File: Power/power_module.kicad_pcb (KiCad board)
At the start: 4 copper layers, 198 x 88 mm, 54 parts, among them J1 Conn_02x03_Odd_Even, J10 Conn_01x04, J11 Conn_02x02_Odd_Even, J2 Conn_02x03_Odd_Even, J3 Conn_02x06_Counter_Clockwise, J4 Conn_02x05_Top_Bottom, J5 Conn_02x05_Top_Bottom, J6 Conn_02x02_Odd_Even, J7 Conn_02x02_Odd_Even, J8 Conn_01x06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

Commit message: Mosfet konumlari degistirildi. Layout iyilestirme yapildi.
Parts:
- moved Q1 22.9 mm to (238.8, 110.5), turned to 270 degrees
- moved D2 16.7 mm to (238.1, 106.5)
- moved R31 12.7 mm to (238.5, 104.1), turned to 180 degrees
- moved D3 11.6 mm to (228.5, 106.6), turned to 180 degrees
- moved R14 11.2 mm to (238.5, 101.7), turned to 0 degrees
- moved Q2 11.0 mm to (227.5, 121.4), turned to 90 degrees
- moved D4 10.2 mm to (241.2, 131.3), turned to 180 degrees
- moved R32 7.43 mm to (228.2, 104.2), turned to 0 degrees
- moved R19 6.72 mm to (228.2, 101.8), turned to 180 degrees
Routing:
- net /CrtPad: track 18.2 -> 83.7 mm
- net GNDA: track 227.4 -> 255.8 mm, vias 10 -> 22
- net /Vout+: track 217.0 -> 234.0 mm
- net Vin_Sens: track 89.9 -> 95.3 mm
- net /Gate2: track 11.3 -> 8.31 mm, vias 0 -> 4
- net /Bridge-: track 121.0 -> 123.8 mm
- net /Gate1: track 12.0 -> 10.6 mm, vias 1 -> 6
- net /Drv_Out: track 14.8 -> 15.6 mm
- net (no net): vias 5 -> 0
- added copper zone on B.Cu, net /CrtPad
- added copper zone on In1.Cu, net /Gate2
- added copper zone on B.Cu, net /Line1
- added copper zone on In2.Cu, net /Line1
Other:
- net class Bridge: clearance 0.8 -> 3
- net class GNDA: clearance 0.3 -> 3
- net class Phase: clearance 0.8 -> 3

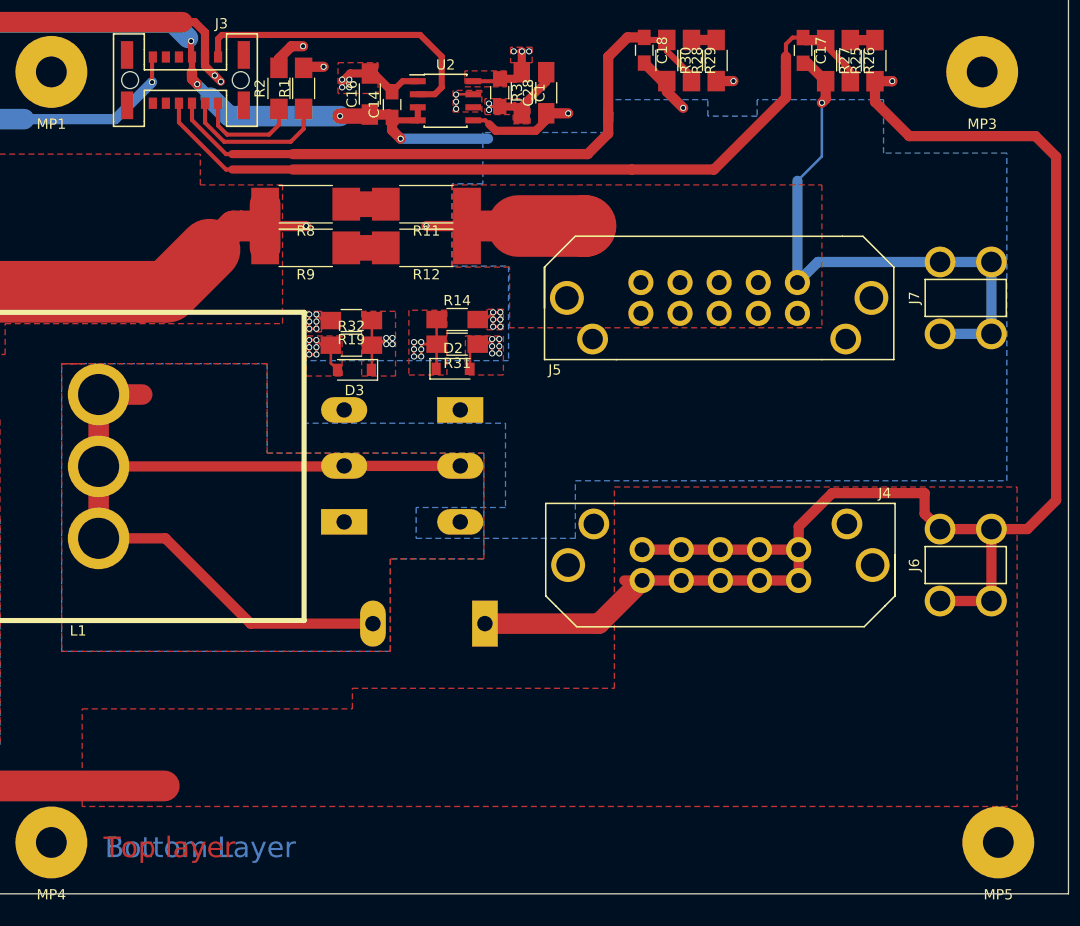
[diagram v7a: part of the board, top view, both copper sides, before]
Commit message: Layout iyilestirmesi. Cikis soketleri kartin sag alt kosesine alindi.
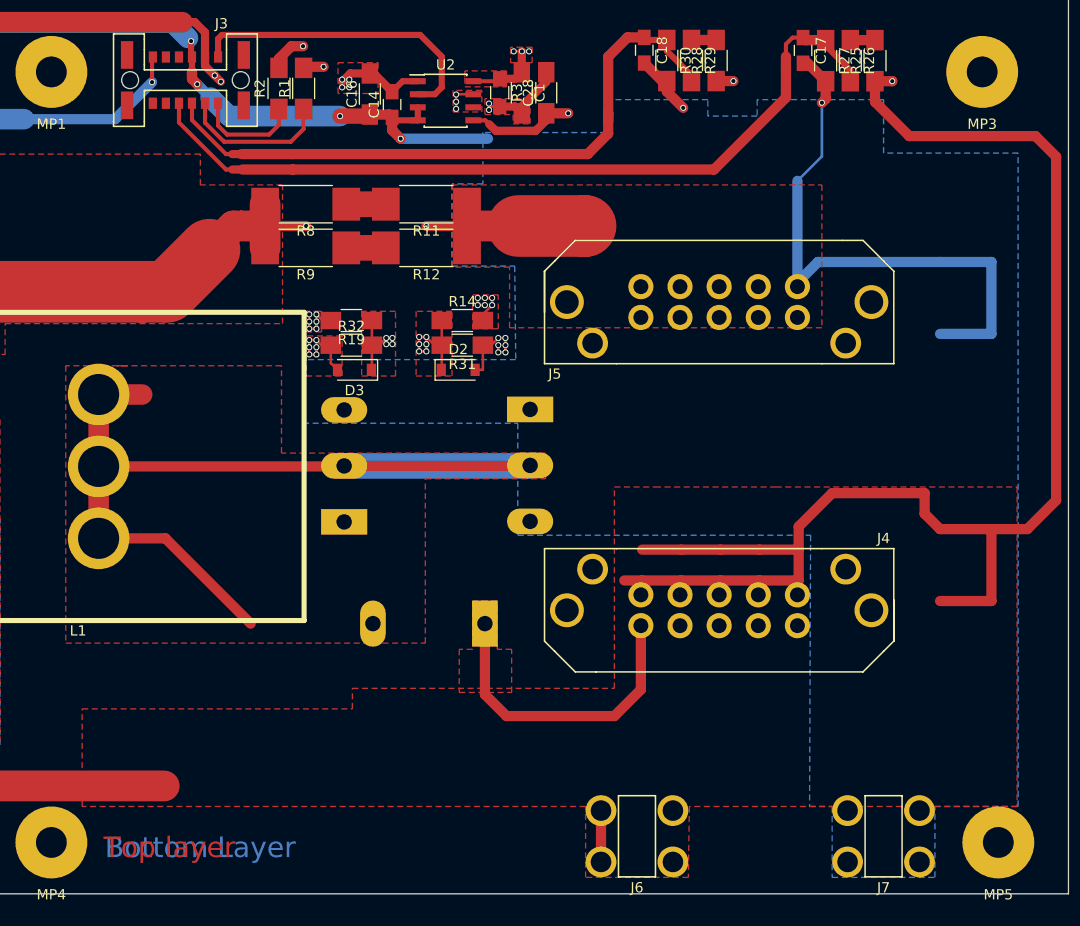
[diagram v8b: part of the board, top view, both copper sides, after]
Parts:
- moved J7 53.0 mm to (280.0, 152.0), turned to 90 degrees
- moved J6 41.5 mm to (256.0, 152.0), turned to 90 degrees
- moved Q1 6.80 mm to (245.6, 110.5)
- moved J4 4.40 mm to (264.0, 130.0)
- moved R31 0.51 mm to (239.0, 104.2)
- moved D2 0.51 mm to (238.6, 106.6)
- moved R14 0.51 mm to (239.0, 101.8)
- moved J5 0.40 mm to (264.0, 100.0)
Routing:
- net /Vout+: track 234.0 -> 252.2 mm
- net /CrtPad: track 83.7 -> 96.7 mm
- net /Drv_Out: track 15.6 -> 13.6 mm
- removed copper zone on B.Cu, net /CrtPad
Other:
- net class PowerTraces: clearance 1 -> 3
